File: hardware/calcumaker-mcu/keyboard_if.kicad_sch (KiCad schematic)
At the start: 1 part, among them J5 TO KEYBOARD

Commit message: hardware: MCU -> STM32U575RGT6 (LQFP-64) + 4MB QSPI flash; monospace wiring notes
MCU package + external flash
- Swap U1 STM32U575ZGT6 (LQFP-144) -> STM32U575RGT6 (LQFP-64, LCSC C5270980).
  The firmware links at ~323 KB so 1 MB flash is ample (~3x headroom), and with
  the key matrix scanned off-board the LQFP-64 has enough GPIO — smaller/cheaper.
- Correct the flash size everywhere: the STM32 `G` code = 1 MB (not 2 MB; the
  `I` parts are 2 MB). memory.x FLASH 2048K -> 1024K; .cargo runner -> RGTx.
- Add U7 W25Q32JVSSIQ, a 4 MB (32 Mbit) quad-SPI NOR (LCSC C179173, SOIC-8) on
  OCTOSPI1 as a new QSPIFlash sheet (+ R9 CS# pull-up + C26 decoupling) for
  memory-mapped (XIP) constants + state/program storage.
- mcu board 52 -> 55 components / 7 sheets. Docs (DESIGN.md, PARTS.md, READMEs,
  CLAUDE/AGENTS) updated; availability ladder now lists RGT6/VGT6/ZGT6.

Monospace, multi-line schematic wiring notes
- kschgen text_note() now renders notes in a monospace font (Courier New) so
  tables/columns line up; add note_block() + pin_table() helpers.
- Reformat all 14 per-sheet notes into titled, multi-line, aligned blocks —
  connector pinouts as PIN/SIGNAL tables, power/MCU sheets as wiring blocks.

The regenerated schematics carry both changes, so this is one commit. All three
boards regenerate + pass the structure check (mcu 55 / keyboard 119 / display
60, no duplicate refs).

Co-Authored-By: Claude Opus 4.8 (1M context) <noreply@anthropic.com>
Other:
- note added: "KEYBOARD MEZZANINE - J5 DF40C-10DS-0.4V (LCSC C424636) Hirose DF40 2x5 0.4mm RECEPTACLE; low-profile 1.5mm stack. Mates the keyboard-board header (kbd J1 DF40C-10DP, C424635). Keyscanning is on the keyboard G0 -> only a serial link + power cross. PLACED, not wired. Both halves MUST agree on this pinout: PIN SIGNAL PIN SIGNAL 1 +3V3 6 KB_UART_RX 2 GND 7 KB_IRQ 3 I2C_SDA 8 KB_NRST 4 I2C_SCL 9 KB_BO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"
- note removed: "Calcumaker 16 MCU — Keyboard mezzanine (J5 = Hirose DF40 2x5 0.4mm RECEPTACLE DF40C-10DS-0.4V, LCSC C424636). The keyboard board stacks ABOVE on this LOW-PROFILE board-to-board pair (mating header = calcumaker-keyboard J1 DF40C-10DP-0.4V C424635; 0.4mm pitch, **1.5mm stack height**). Keyscanning lives on the KEYBOARD board's STM32G0, so only a serial link + power cross here. PLACED, not wired. PI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"
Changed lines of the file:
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@@
 	(title_block
 		(title "Calcumaker 16 — MCU — Keyboard mezzanine (I2C + UART link to the stacked keyboard)")
-		(date "2026-07-05")
-		(rev "0.2")
+		(date "2026-07-06")
+		(rev "0.3")
 		(company "calcumaker authors")
 	)
@@
 		(instances
 			(project "calcumaker-mcu"
-				(path "/ca1c0000-0000-4000-8000-00000000ma01/f3eb8744-2884-4df4-9891-07d87447427d"
+				(path "/ca1c0000-0000-4000-8000-00000000ma01/32aa4625-0e65-45ea-b771-87030b782539"
 					(reference "J5")
 					(unit 1)
@@
 		)
 	)
-	(text "Calcumaker 16 MCU — Keyboard mezzanine (J5 = Hirose DF40 2x5 0.4mm RECEPTACLE DF40C-10DS-0.4V, LCSC C424636). The keyboard board stacks ABOVE on this LOW-PROFILE board-to-board pair (mating header = calcumaker-keyboard J1 DF40C-10DP-0.4V C424635; 0.4mm pitch, **1.5mm stack height**). Keyscanning lives on the KEYBOARD board's STM32G0, so only a serial link + power cross here. PLACED, not wired. PINOUT (both halves MUST agree): 1=+3V3, 2=GND, 3=I2C_SDA, 4=I2C_SCL, 5=KB_UART_TX, 6=KB_UART_RX, 7=KB_IRQ, 8=KB_NRST, 9=KB_BOOT0, 10=GND. I2C = the G0 reports (row,col) events; KB_IRQ -> a MCU WKUP pin wakes the U575 on a keypress; UART = alt/expansion + the G0's ROM/DFU bootloader; KB_NRST/KB_BOOT0 let the MCU reflash the G0. MECH: at a 1.5mm stack the MX pins under the keyboard (~2-3mm) can't sit over the MCU board — keep the MCU board under a keyless region (or trim pins); keep USB-C/battery at the board EDGE. Verify DF40C-10DS land vs the KiCad DF40 2x5 footprint + the 3D stack at layout. See DESIGN.md Board Partition + Low-power & wake."
+	(text "KEYBOARD MEZZANINE  -  J5  DF40C-10DS-0.4V  (LCSC C424636)\nHirose DF40 2x5 0.4mm RECEPTACLE; low-profile 1.5mm stack.\nMates the keyboard-board header (kbd J1 DF40C-10DP, C424635).\nKeyscanning is on the keyboard G0 -> only a serial link + power cross.\nPLACED, not wired.  Both halves MUST agree on this pinout:\n\n  PIN  SIGNAL        PIN  SIGNAL    \n    1  +3V3            6  KB_UART_RX\n    2  GND             7  KB_IRQ    \n    3  I2C_SDA         8  KB_NRST   \n    4  I2C_SCL         9  KB_BOOT0  \n    5  KB_UART_TX     10  GND\n\nI2C     G0 reports (row,col) events + gets annunciator state.\nKB_IRQ  G0 -> a MCU WKUP pin: wakes the U575 on a keypress.\nUART    alt/expansion + the G0 ROM/DFU bootloader.\nNRST/BOOT0  let the MCU reflash the G0.\n\nMECH: 1.5mm stack < MX pin protrusion (~2-3mm) -> keep the MCU board\nunder a keyless region (or trim pins); USB-C/battery at the board EDGE.\nVerify DF40C-10DS land vs the KiCad DF40 2x5 fp + 3D stack at layout."
 		(exclude_from_sim no)
 		(at 15.00 105.00 0)
-		(effects (font (size 1.5 1.5)) (justify left top))
+		(effects (font (face "Courier New") (size 1.27 1.27)) (justify left top))
 	)
 	(sheet_instances

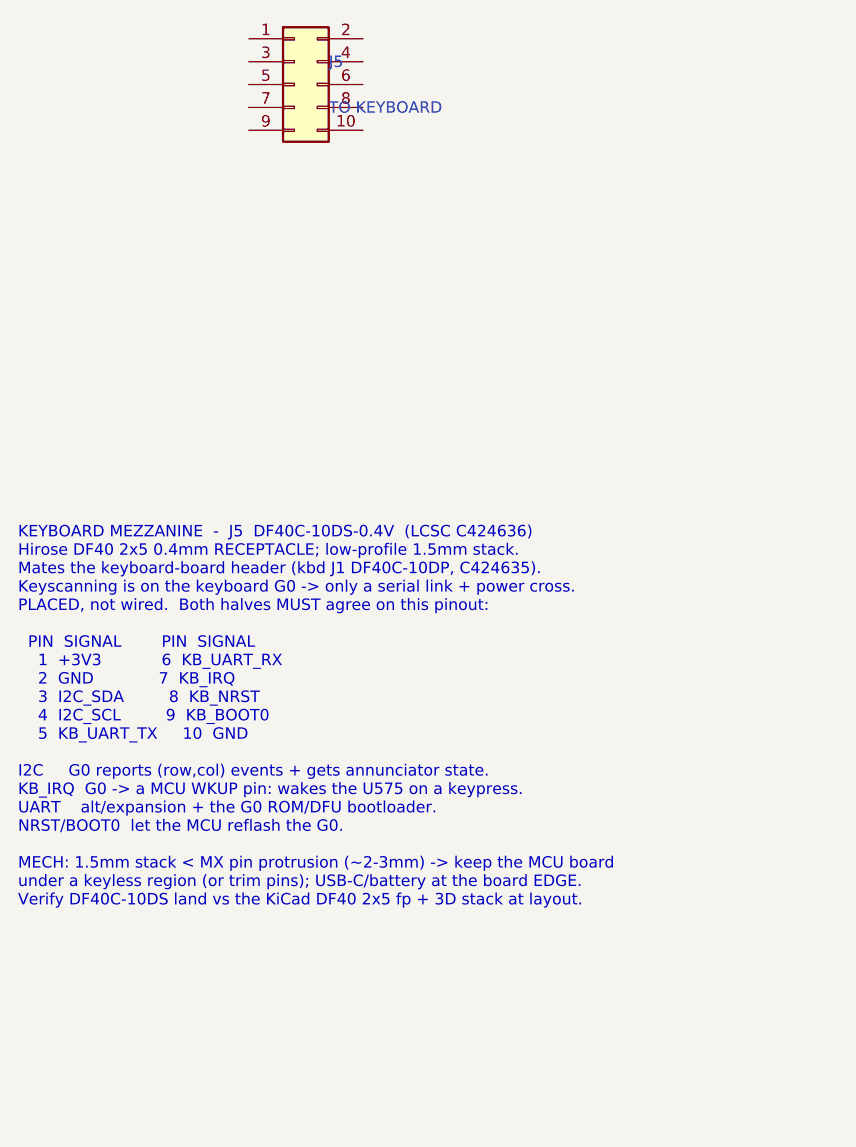
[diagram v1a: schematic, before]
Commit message: hardware: per-key RGB hint lighting on the keyboard board (50x SK6805 on gated VSYS) (#4)
Add addressable RGB accent lighting that hints key positions / presses -- one
SK6805-EC15 (1.5x1.5mm, the smallest serial RGB with a KiCad footprint + real
LCSC stock, C2890035) beside each of the 50 keys, single-wire daisy chain off
one STM32G0 pin.

Power: the LEDs are ~5V parts and the keyboard rail is only 3.3V, so they run
off VSYS (the MCU board's load-shared battery/USB rail, ~3.7-4.7V) brought up a
WIDENED 12-pin mezzanine (10 -> 12: +VSYS +GND). A high-side P-FET load switch
(Q1 AO3401A + Q2 2N7002) gates the whole LED rail off in sleep (G0 LED_EN) to
protect battery life, and a 74LVC1G125 (powered from the gated rail) level-shifts
the 3.3V data up to the LED VIH.

- calcumaker-keyboard: new KeyLighting sheet (50x SK6805 D56-D105 + U2 shifter +
  Q1/Q2 load switch + R7-R10 / C6-C7); J1 mezzanine -> 12-pin DF40C-12DP
  (C6224952). 119 -> 178 components.
- calcumaker-mcu: J5 mezzanine -> 12-pin DF40B-12DS (C3641147); route VSYS.
- DF40 stack: the receptacle SUFFIX sets the mated height (none = 1.5mm,
  (2.0) = 2.0mm, H-series = 2.5-4.0mm), NOT the B/C letter; the DF40C plug is the
  common header -- so DF40C-12DP x DF40B-12DS is a valid 1.5mm stack, same as the
  original 10-pin (DF40C-12DS just isn't LCSC-stocked).
- DESIGN.md / PARTS.md / memory: RGB subsystem, 12-pin pinout, BOM rows, the
  sleep-gate + current-cap notes (firmware must cap total brightness; 50x
  full-white ~0.75A would exceed the DF40 / VSYS budget).

All three boards regenerate + pass the structure check (mcu 55 / keyboard 178 /
display 60, no duplicate refs).

Co-authored-by: Claude Opus 4.8 (1M context) <noreply@anthropic.com>
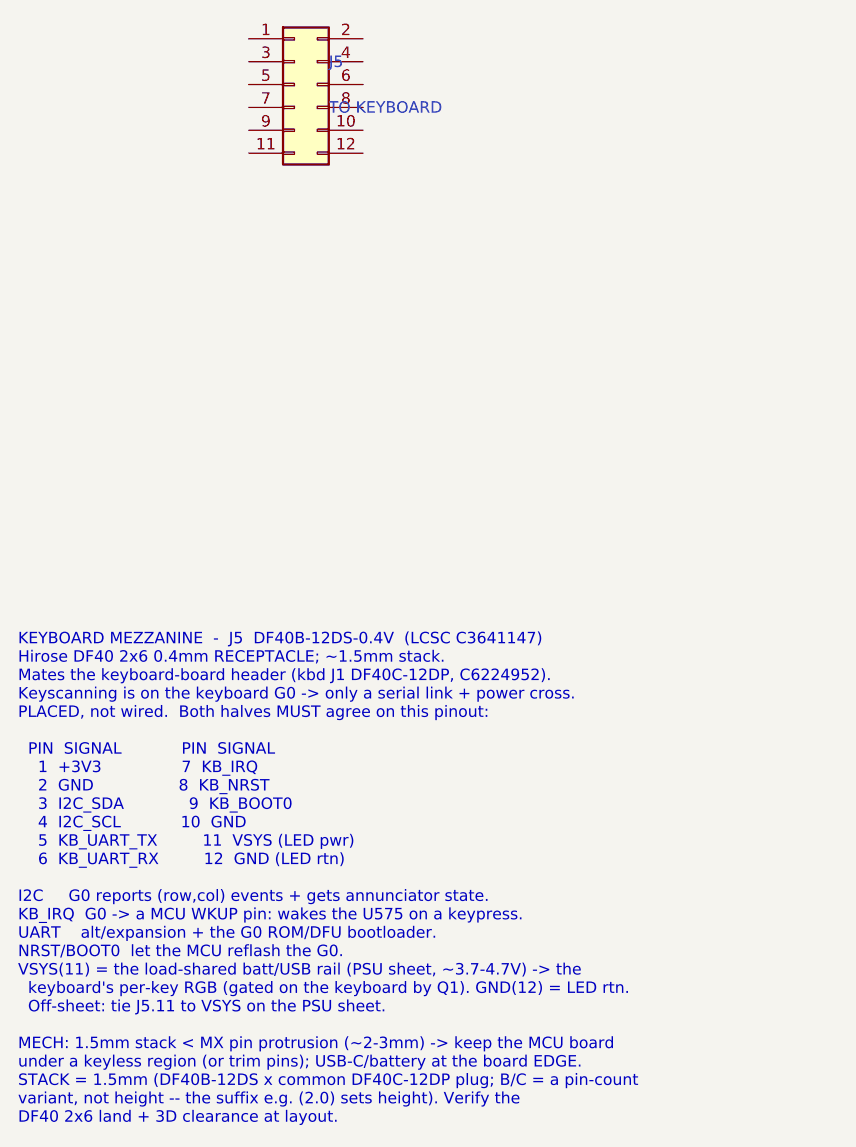
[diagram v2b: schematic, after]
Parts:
- removed J5: TO KEYBOARD, Connector_Hirose_DF40:Hirose_DF40B-10DS-0.4V_2x05-1MP_P0.4mm, symbol Connector_Generic:Conn_02x05_Odd_Even
- added J5: TO KEYBOARD, Connector_Hirose_DF40:Hirose_DF40B-12DS-0.4V_2x06-1MP_P0.4mm, symbol Connector_Generic:Conn_02x06_Odd_Even
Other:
- note added: "KEYBOARD MEZZANINE - J5 DF40B-12DS-0.4V (LCSC C3641147) Hirose DF40 2x6 0.4mm RECEPTACLE; ~1.5mm stack. Mates the keyboard-board header (kbd J1 DF40C-12DP, C6224952). Keyscanning is on the keyboard G0 -> only a serial link + power cross. PLACED, not wired. Both halves MUST agree on this pinout: PIN SIGNAL PIN SIGNAL 1 +3V3 7 KB_IRQ 2 GND 8 KB_NRST 3 I2C_SDA 9 KB_BOOT0 4 I2C_SCL 10 GND 5 KB_UART_T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"
- note removed: "KEYBOARD MEZZANINE - J5 DF40C-10DS-0.4V (LCSC C424636) Hirose DF40 2x5 0.4mm RECEPTACLE; low-profile 1.5mm stack. Mates the keyboard-board header (kbd J1 DF40C-10DP, C424635). Keyscanning is on the keyboard G0 -> only a serial link + power cross. PLACED, not wired. Both halves MUST agree on this pinout: PIN SIGNAL PIN SIGNAL 1 +3V3 6 KB_UART_RX 2 GND 7 KB_IRQ 3 I2C_SDA 8 KB_NRST 4 I2C_SCL 9 KB_BO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"
- title: Calcumaker 16 — MCU — Keyboard mezzanine (I2C + UART link to the stacked keyboard) -> Calcumaker 16 — MCU — Keyboard mezzanine (I2C + UART + VSYS to the stacked keyboard)
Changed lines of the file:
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@@
 	(paper "A3")
 	(title_block
-		(title "Calcumaker 16 — MCU — Keyboard mezzanine (I2C + UART link to the stacked keyboard)")
+		(title "Calcumaker 16 — MCU — Keyboard mezzanine (I2C + UART + VSYS to the stacked keyboard)")
 		(date "2026-07-06")
 		(rev "0.3")
@@
 	)
 	(symbol
-		(lib_id "Connector_Generic:Conn_02x05_Odd_Even")
+		(lib_id "Connector_Generic:Conn_02x06_Odd_Even")
 		(at 45.7200 55.8800 0)
 		(unit 1)
@@
 			(effects (font (size 1.27 1.27)) (justify left))
 		)
-		(property "Footprint" "Connector_Hirose_DF40:Hirose_DF40B-10DS-0.4V_2x05-1MP_P0.4mm"
+		(property "Footprint" "Connector_Hirose_DF40:Hirose_DF40B-12DS-0.4V_2x06-1MP_P0.4mm"
 			(at 45.7200 55.8800 0)
 			(effects (font (size 1.27 1.27))) (hide yes)
@@
 			(effects (font (size 1.27 1.27))) (hide yes)
 		)
-		(property "LCSC" "C424636"
+		(property "LCSC" "C3641147"
 			(at 45.7200 55.8800 0)
 			(effects (font (size 1.27 1.27))) (hide yes)
 		)
-		(property "MPN" "DF40C-10DS-0.4V(51)"
+		(property "MPN" "DF40B-12DS-0.4V(58)"
 			(at 45.7200 55.8800 0)
 			(effects (font (size 1.27 1.27))) (hide yes)
@@
 		(pin "9")
 		(pin "10")
+		(pin "11")
+		(pin "12")
 		(instances
 			(project "calcumaker-mcu"
@@
 		)
 	)
-	(text "KEYBOARD MEZZANINE  -  J5  DF40C-10DS-0.4V  (LCSC C424636)\nHirose DF40 2x5 0.4mm RECEPTACLE; low-profile 1.5mm stack.\nMates the keyboard-board header (kbd J1 DF40C-10DP, C424635).\nKeyscanning is on the keyboard G0 -> only a serial link + power cross.\nPLACED, not wired.  Both halves MUST agree on this pinout:\n\n  PIN  SIGNAL        PIN  SIGNAL    \n    1  +3V3            6  KB_UART_RX\n    2  GND             7  KB_IRQ    \n    3  I2C_SDA         8  KB_NRST   \n    4  I2C_SCL         9  KB_BOOT0  \n    5  KB_UART_TX     10  GND\n\nI2C     G0 reports (row,col) events + gets annunciator state.\nKB_IRQ  G0 -> a MCU WKUP pin: wakes the U575 on a keypress.\nUART    alt/expansion + the G0 ROM/DFU bootloader.\nNRST/BOOT0  let the MCU reflash the G0.\n\nMECH: 1.5mm stack < MX pin protrusion (~2-3mm) -> keep the MCU board\nunder a keyless region (or trim pins); USB-C/battery at the board EDGE.\nVerify DF40C-10DS land vs the KiCad DF40 2x5 fp + 3D stack at layout."
+	(text "KEYBOARD MEZZANINE  -  J5  DF40B-12DS-0.4V  (LCSC C3641147)\nHirose DF40 2x6 0.4mm RECEPTACLE; ~1.5mm stack.\nMates the keyboard-board header (kbd J1 DF40C-12DP, C6224952).\nKeyscanning is on the keyboard G0 -> only a serial link + power cross.\nPLACED, not wired.  Both halves MUST agree on this pinout:\n\n  PIN  SIGNAL            PIN  SIGNAL        \n    1  +3V3                7  KB_IRQ        \n    2  GND                 8  KB_NRST       \n    3  I2C_SDA             9  KB_BOOT0      \n    4  I2C_SCL            10  GND           \n    5  KB_UART_TX         11  VSYS (LED pwr)\n    6  KB_UART_RX         12  GND (LED rtn)\n\nI2C     G0 reports (row,col) events + gets annunciator state.\nKB_IRQ  G0 -> a MCU WKUP pin: wakes the U575 on a keypress.\nUART    alt/expansion + the G0 ROM/DFU bootloader.\nNRST/BOOT0  let the MCU reflash the G0.\nVSYS(11) = the load-shared batt/USB rail (PSU sheet, ~3.7-4.7V) -> the\n  keyboard's per-key RGB (gated on the keyboard by Q1). GND(12) = LED rtn.\n  Off-sheet: tie J5.11 to VSYS on the PSU sheet.\n\nMECH: 1.5mm stack < MX pin protrusion (~2-3mm) -> keep the MCU board\nunder a keyless region (or trim pins); USB-C/battery at the board EDGE.\nSTACK = 1.5mm (DF40B-12DS x common DF40C-12DP plug; B/C = a pin-count\nvariant, not height -- the suffix e.g. (2.0) sets height). Verify the\nDF40 2x6 land + 3D clearance at layout."
 		(exclude_from_sim no)
-		(at 15.00 105.00 0)
+		(at 15.00 116.88 0)
 		(effects (font (face "Courier New") (size 1.27 1.27)) (justify left top))
 	)
